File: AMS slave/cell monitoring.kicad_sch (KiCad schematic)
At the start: 80 parts, among them J1 559010274, Q1 KY2N7002, SW1 SW_Push, U1 BQ76940DBT

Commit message: Functionable AMS slave 1.0.0
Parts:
- added D10, D11, D12, D13, D14, D15, D16, D17, D18, D19, D20, D7, D8, D9: BZT52B5V1, to be sorted:D_SOD-123F, symbol Device:D_Zener
- added Q1, Q10, Q11, Q12, Q13, Q14, Q2, Q3, Q4, Q5, Q6, Q7, Q8, Q9: DMG1012UW, Package_TO_SOT_SMD:SOT-323_SC-70, symbol Transistor_FET:Q_NMOS_GSD
- added R23, R24, R25, R26, R43, R44, R45, R46, R47, R48, R49, R50, R51, R52, R53: 10k, RMC_Resistor:R_0805_2012Metric_Pad1.20x1.40mm_HandSolder_L, symbol Device:R
- added RBAL1, RBAL10, RBAL11, RBAL12, RBAL13, RBAL14, RBAL2, RBAL3, RBAL4, RBAL5, RBAL6, RBAL7, RBAL8, RBAL9: 10R, RMC_Resistor:R_1206_3216Metric_Pad1.30x1.75mm_HandSolder_RMC, symbol Device:R
- added U5: LTV-817S, Package_DIP:SMDIP-4_W9.53mm, symbol Isolator:LTV-817S
- BT1, BT10, BT11, BT12, BT13, BT14, BT2, BT3, BT4, BT5, BT6, BT7, BT8, BT9: now fitted
- renumbered Q1 to Q15
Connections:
- net +3V3: no longer RBOOT1.1
- net BQ_BOOT: now also R44.1
- net GND: now also Q1.2 (S)
- net PACK+: now also D20.1 (K), RBAL14.1
- net TP1: now also RBOOT1.1, D7.1 (K), Q2.2 (S), RBAL1.1, U5.4
- net TP10: now also D16.1 (K), Q11.2 (S), RBAL10.1
- net TP11: now also D17.1 (K), Q12.2 (S), RBAL11.1
- net TP12: now also D18.1 (K), Q13.2 (S), RBAL12.1
- net TP13: now also D19.1 (K), Q14.2 (S), RBAL13.1
- net TP2: now also D8.1 (K), Q3.2 (S), RBAL2.1
- net TP3: now also D9.1 (K), Q4.2 (S), RBAL3.1
- net TP4: now also D10.1 (K), Q5.2 (S), RBAL4.1
- net TP5: now also D11.1 (K), Q6.2 (S), RBAL5.1
- net TP6: now also D12.1 (K), Q7.2 (S), RBAL6.1
- net TP7: now also D13.1 (K), Q8.2 (S), RBAL7.1
- net TP8: now also D14.1 (K), Q9.2 (S), RBAL8.1
- net TP9: now also D15.1 (K), Q10.2 (S), RBAL9.1
- net VC1: now also R23.2
- net VC10: now also R49.2
- net VC11: now also R50.2
- net VC12: now also R51.2
- net VC13: now also R52.2
- net VC15: now also R53.2
- net VC2: now also R24.2
- net VC3: now also R25.2
- net VC4: now also R26.2
- net VC5: now also R43.2
- net VC6: now also R45.2
- net VC7: now also R46.2
- net VC8: now also R47.2
- net VC9: now also R48.2
- new net: Q9.3 (D), RBAL9.2
- new net: D14.2 (A), Q8.1 (G), R47.1
- new net: Q5.3 (D), RBAL5.2
- new net: D9.2 (A), Q3.1 (G), R25.1
- new net: D8.2 (A), Q2.1 (G), R24.1
- new net: D18.2 (A), Q12.1 (G), R51.1
- new net: Q12.3 (D), RBAL12.2
- new net: D16.2 (A), Q10.1 (G), R49.1
- new net: D17.2 (A), Q11.1 (G), R50.1
- new net: D10.2 (A), Q4.1 (G), R26.1
- new net: D7.2 (A), Q1.1 (G), R23.1
- new net: Q2.3 (D), RBAL2.2
- new net: D13.2 (A), Q7.1 (G), R46.1
- new net: Q8.3 (D), RBAL8.2
- new net: Q1.3 (D), RBAL1.2
- new net: D15.2 (A), Q9.1 (G), R48.1
- new net: D11.2 (A), Q5.1 (G), R43.1
- new net: Q13.3 (D), RBAL13.2
- new net: Q11.3 (D), RBAL11.2
- new net: D12.2 (A), Q6.1 (G), R45.1
- new net: D19.2 (A), Q13.1 (G), R52.1
- new net: Q14.3 (D), RBAL14.2
- new net: R44.2, U5.3
- new net: Q7.3 (D), RBAL7.2
- new net: D20.2 (A), Q14.1 (G), R53.1
- new net: Q3.3 (D), RBAL3.2
- new net: Q4.3 (D), RBAL4.2
- new net: Q10.3 (D), RBAL10.2
- new net: Q6.3 (D), RBAL6.2
- new net GND2: U5.2
- new net VCC2: U5.1
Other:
- moved on the sheet: C1, C10, C11, C12, C13, C14, C2, C3, C4, C5, C6, C7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

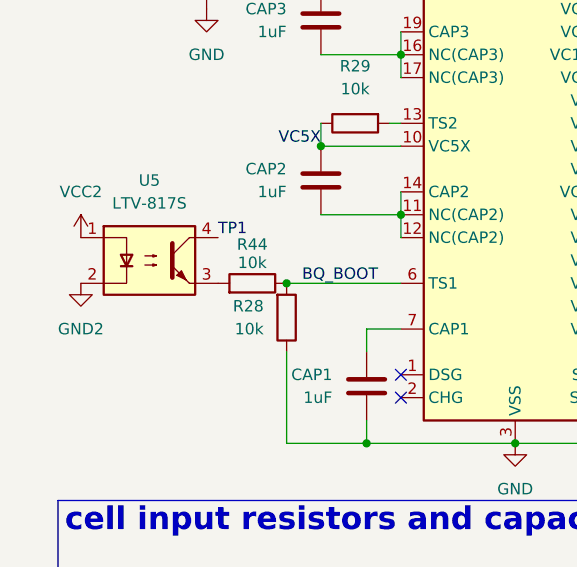
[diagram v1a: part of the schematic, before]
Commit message: AMS slave that actually is functionable
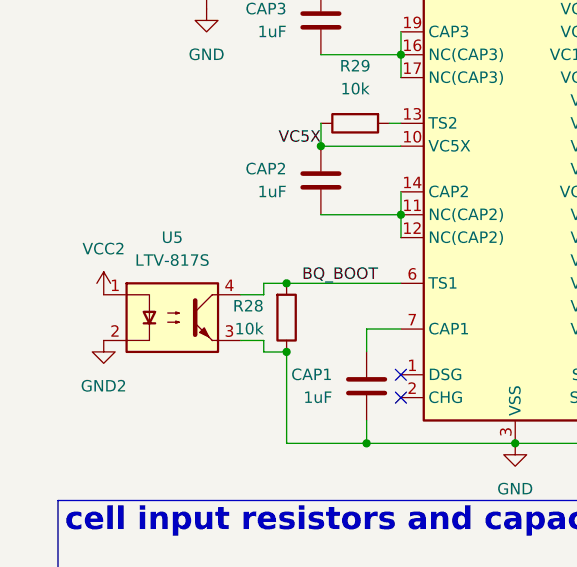
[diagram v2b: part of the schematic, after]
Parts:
- removed R44: 10k, RMC_Resistor:R_0805_2012Metric_Pad1.20x1.40mm_HandSolder_L, symbol Device:R
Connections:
- net BQ_BOOT: now also U5.4
- net GND: now also U5.3
- net TP1: no longer U5.4
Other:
- moved on the sheet: U5
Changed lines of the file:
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@@
 	)
 	(junction
+		(at 38.1 87.63)
+		(diameter 0)
+		(color 0 0 0 0)
+	)
+	(junction
 		(at 41.91 64.77)
 		(diameter 0)
@@
 	)
 	(junction
-		(at 38.1 80.01)
-		(diameter 0)
-		(color 0 0 0 0)
-	)
-	(junction
 		(at 218.44 157.48)
 		(diameter 0)
@@
 	)
 	(junction
+		(at 38.1 80.01)
+		(diameter 0)
+		(color 0 0 0 0)
+	)
+	(junction
 		(at 274.32 157.48)
 		(diameter 0)
@@
 	(wire
 		(pts
+			(xy 35.56 87.63) (xy 38.1 87.63)
+		)
+		(stroke
+			(width 0)
+			(type default)
+		)
+	)
+	(wire
+		(pts
 			(xy 134.62 151.13) (xy 134.62 153.67)
 		)
@@
 	(wire
 		(pts
+			(xy 35.56 81.28) (xy 35.56 80.01)
+		)
+		(stroke
+			(width 0)
+			(type default)
+		)
+	)
+	(wire
+		(pts
 			(xy 25.4 165.1) (xy 27.94 165.1)
 		)
@@
 	(wire
 		(pts
+			(xy 33.02 81.28) (xy 35.56 81.28)
+		)
+		(stroke
+			(width 0)
+			(type default)
+		)
+	)
+	(wire
+		(pts
 			(xy 121.92 55.88) (xy 121.92 69.85)
 		)
@@
 	(wire
 		(pts
+			(xy 33.02 86.36) (xy 35.56 86.36)
+		)
+		(stroke
+			(width 0)
+			(type default)
+		)
+	)
+	(wire
+		(pts
 			(xy 135.89 62.23) (xy 133.35 62.23)
 		)
@@
 	(wire
 		(pts
+			(xy 35.56 86.36) (xy 35.56 87.63)
+		)
+		(stroke
+			(width 0)
+			(type default)
+		)
+	)
+	(wire
+		(pts
 			(xy 242.57 45.72) (xy 242.57 52.07)
 		)
@@
 	(wire
 		(pts
+			(xy 35.56 80.01) (xy 38.1 80.01)
+		)
+		(stroke
+			(width 0)
+			(type default)
+		)
+	)
+	(wire
+		(pts
 			(xy 25.4 175.26) (xy 25.4 177.8)
 		)
@@
 		)
 	)
-	(label "TP1"
-		(at 30.48 74.93 0)
-		(effects
-			(font
-				(size 1.27 1.27)
-			)
-			(justify left bottom)
-		)
-	)
 	(hierarchical_label "NTC5+"
 		(shape output)
@@
 	(symbol
 		(lib_id "power:VCC")
-		(at 15.24 74.93 0)
+		(at 17.78 81.28 0)
 		(unit 1)
 		(body_style 1)
@@
 		(fields_autoplaced yes)
 		(property "Reference" "#PWR036"
-			(at 15.24 78.74 0)
+			(at 17.78 85.09 0)
 			(hide yes)
 			(show_name no)
@@
 		)
 		(property "Value" "VCC2"
-			(at 15.24 69.85 0)
+			(at 17.78 76.2 0)
 			(show_name no)
 			(do_not_autoplace no)
@@
 		)
 		(property "Footprint" ""
-			(at 15.24 74.93 0)
+			(at 17.78 81.28 0)
 			(hide yes)
 			(show_name no)
@@
 		)
 		(property "Datasheet" ""
-			(at 15.24 74.93 0)
+			(at 17.78 81.28 0)
 			(hide yes)
 			(show_name no)
@@
 		)
 		(property "Description" "Power symbol creates a global label with name \"VCC\""
-			(at 15.24 74.93 0)
+			(at 17.78 81.28 0)
 			(hide yes)
 			(show_name no)
@@
 	)
 	(symbol
-		(lib_id "Device:R")
-		(at 34.29 80.01 270)
-		(mirror x)
-		(unit 1)
-		(body_style 1)
-		(exclude_from_sim no)
-		(in_bom yes)
-		(on_board yes)
-		(in_pos_files yes)
-		(dnp no)
-		(property "Reference" "R44"
-			(at 34.29 75.692 90)
-			(show_name no)
-			(do_not_autoplace no)
-			(effects
-				(font
-					(size 1.27 1.27)
-				)
-			)
-		)
-		(property "Value" "10k"
-			(at 34.29 77.724 90)
-			(show_name no)
-			(do_not_autoplace no)
-			(effects
-				(font
-					(size 1.27 1.27)
-				)
-			)
-		)
-		(property "Footprint" "RMC_Resistor:R_0805_2012Metric_Pad1.20x1.40mm_HandSolder_L"
-			(at 34.29 81.788 90)
-			(hide yes)
-			(show_name no)
-			(do_not_autoplace no)
-			(effects
-				(font
-					(size 1.27 1.27)
-				)
-			)
-		)
-		(property "Datasheet" ""
-			(at 34.29 80.01 0)
-			(hide yes)
-			(show_name no)
-			(do_not_autoplace no)
-			(effects
-				(font
-					(size 1.27 1.27)
-				)
-			)
-		)
-		(property "Description" "Resistor"
-			(at 34.29 80.01 0)
-			(hide yes)
-			(show_name no)
-			(do_not_autoplace no)
-			(effects
-				(font
-					(size 1.27 1.27)
-				)
-			)
-		)
-		(pin "2"
-		)
-		(pin "1"
-		)
-		(instances
-			(project "AMS slave"
-				(path "/9d086174-c3f9-4f2b-b5ac-a2d10e7f2013/72ba2d86-b5f1-4c9f-9e37-5b2b76178c75"
-					(reference "R44")
-					(unit 1)
-				)
-			)
-		)
-	)
-	(symbol
 		(lib_id "Transistor_FET:Q_NMOS_GSD")
 		(at 111.76 160.02 0)
@@
 	(symbol
 		(lib_id "power:GND2")
-		(at 15.24 80.01 0)
+		(at 17.78 86.36 0)
 		(unit 1)
 		(body_style 1)
@@
 		(fields_autoplaced yes)
 		(property "Reference" "#PWR037"
-			(at 15.24 86.36 0)
+			(at 17.78 92.71 0)
 			(hide yes)
 			(show_name no)
@@
 		)
 		(property "Value" "GND2"
-			(at 15.24 85.09 0)
+			(at 17.78 91.44 0)
 			(show_name no)
 			(do_not_autoplace no)
@@
 		)
 		(property "Footprint" ""
-			(at 15.24 80.01 0)
+			(at 17.78 86.36 0)
 			(hide yes)
 			(show_name no)
@@
 		)
 		(property "Datasheet" ""
-			(at 15.24 80.01 0)
+			(at 17.78 86.36 0)
 			(hide yes)
 			(show_name no)
@@
 		)
 		(property "Description" "Power symbol creates a global label with name \"GND2\" , ground"
-			(at 15.24 80.01 0)
+			(at 17.78 86.36 0)
 			(hide yes)
 			(show_name no)
@@
 	(symbol
 		(lib_id "Isolator:LTV-817S")
-		(at 22.86 77.47 0)
+		(at 25.4 83.82 0)
 		(unit 1)
 		(body_style 1)
@@
 		(fields_autoplaced yes)
 		(property "Reference" "U5"
-			(at 22.86 68.58 0)
+			(at 25.4 74.93 0)
 			(show_name no)
 			(do_not_autoplace no)
@@
 		)
 		(property "Value" "LTV-817S"
-			(at 22.86 71.12 0)
+			(at 25.4 77.47 0)
 			(show_name no)
 			(do_not_autoplace no)
@@
 		)
 		(property "Footprint" "Package_DIP:SMDIP-4_W9.53mm"
-			(at 22.86 85.09 0)
+			(at 25.4 91.44 0)
 			(hide yes)
 			(show_name no)
@@
 		)
 		(property "Datasheet" "http://www.us.liteon.com/downloads/LTV-817-827-847.PDF"
-			(at 13.97 69.85 0)
+			(at 16.51 76.2 0)
 			(hide yes)
 			(show_name no)
@@
 		)
 		(property "Description" "DC Optocoupler, Vce 35V, CTR 50%, SMDIP-4"
-			(at 22.86 77.47 0)
+			(at 25.4 83.82 0)
 			(hide yes)
 			(show_name no)
